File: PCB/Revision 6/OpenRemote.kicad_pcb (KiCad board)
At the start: 2 copper layers, 192.4 x 50 mm, 191 parts, among them J1 USB_C_Receptacle_USB2.0, J2 Conn_01x50, J3 JST_PH_B2B-PH, J4 2.54x2 Header, J5 Micro_SD_Card, Q1 DMG2301L, Q2 MBT3904DW1, Q3 DMG2301L, Q4 DMG2301L, Q5 DMG2301L, Q6 FS8205A, Q7 DMG2301L, U1 DW01A, U10 APX803S, U11 TP4056, U12 TCA8418, U2 XC6220B331, U3 CH340C, U4 USBLC6-2P6, U5 LIS3DHTR, U6 TSSP77038, U7 ESP32-S3-WROOM-1-N16R8, U8 AP2112K-3.3, U9 MAX17048G

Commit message: Add headerless microphone 3D model
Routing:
- net SW_D: track 78.1 -> 73.3 mm, vias 3 -> 1
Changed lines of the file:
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@@
 		)
 		(fp_text user "ACOUSTIC PORT"
-			(at 0 -3.9 90)
-			(layer "F.Fab")
+			(at 0 2.5 270)
+			(layer "B.SilkS")
 			(effects
 				(font
@@
 					(thickness 0.12)
 				)
+				(justify mirror)
 			)
 		)
@@
 		)
 		(embedded_fonts no)
+		(model "${KIPRJMOD}/project_libraries/3D-models/MS3625_Circular_Microphone_Module_No_Headers.step"
+			(offset
+				(xyz 0 0 0)
+			)
+			(scale
+				(xyz 1 1 1)
+			)
+			(rotate
+				(xyz -90 -0 -180)
+			)
+		)
 	)
 	(footprint "Resistor_SMD:R_0603_1608Metric"
@@
 	)
 	(segment
-		(start 140.5 117)
-		(end 138.5 115)
-		(width 0.3)
-		(layer "F.Cu")
-		(net "SW_D")
-	)
-	(segment
 		(start 131.25 118.6)
 		(end 131.8 118.6)
@@
 		(net "SW_D")
 	)
-	(segment
-		(start 140.5 117.5)
-		(end 140.5 117)
-		(width 0.3)
-		(layer "F.Cu")
-		(net "SW_D")
-	)
 	(via
 		(at 131.8 118.6)
@@
 		(net "SW_D")
 	)
-	(via
-		(at 140.5 117.5)
-		(size 0.8)
-		(drill 0.4)
-		(layers "F.Cu" "B.Cu")
-		(net "SW_D")
-	)
-	(via
-		(at 138.5 115)
-		(size 0.8)
-		(drill 0.4)
-		(layers "F.Cu" "B.Cu")
-		(net "SW_D")
-	)
-	(segment
-		(start 139.526677 118.6)
-		(end 140.5 117.626677)
-		(width 0.3)
-		(layer "B.Cu")
-		(net "SW_D")
-	)
 	(segment
 		(start 140.275 108.225)
@@
 		(width 0.3)
 		(layer "B.Cu")
-		(net "SW_D")
-	)
-	(segment
-		(start 140.5 117.626677)
-		(end 140.5 117.5)
-		(width 0.3)
-		(layer "B.Cu")

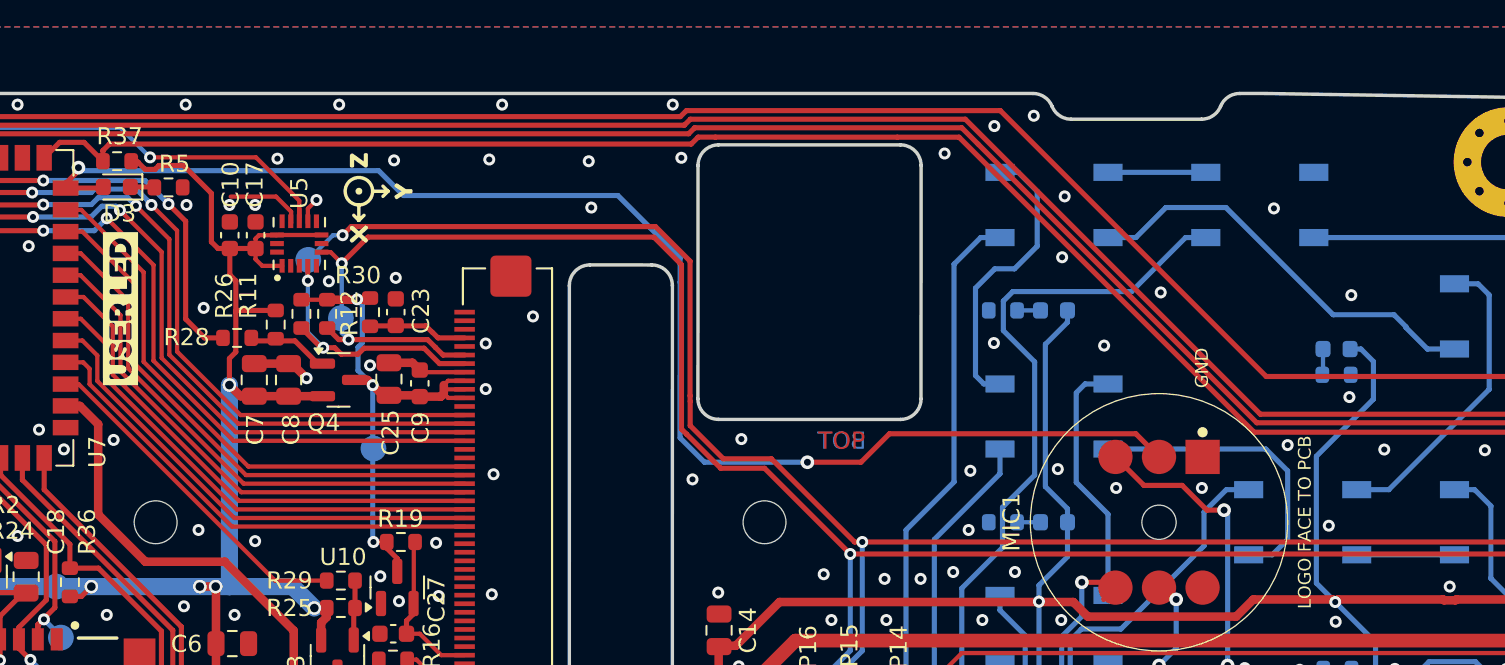
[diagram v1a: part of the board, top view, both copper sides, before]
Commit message: Add Rev 6 microphone and display updates
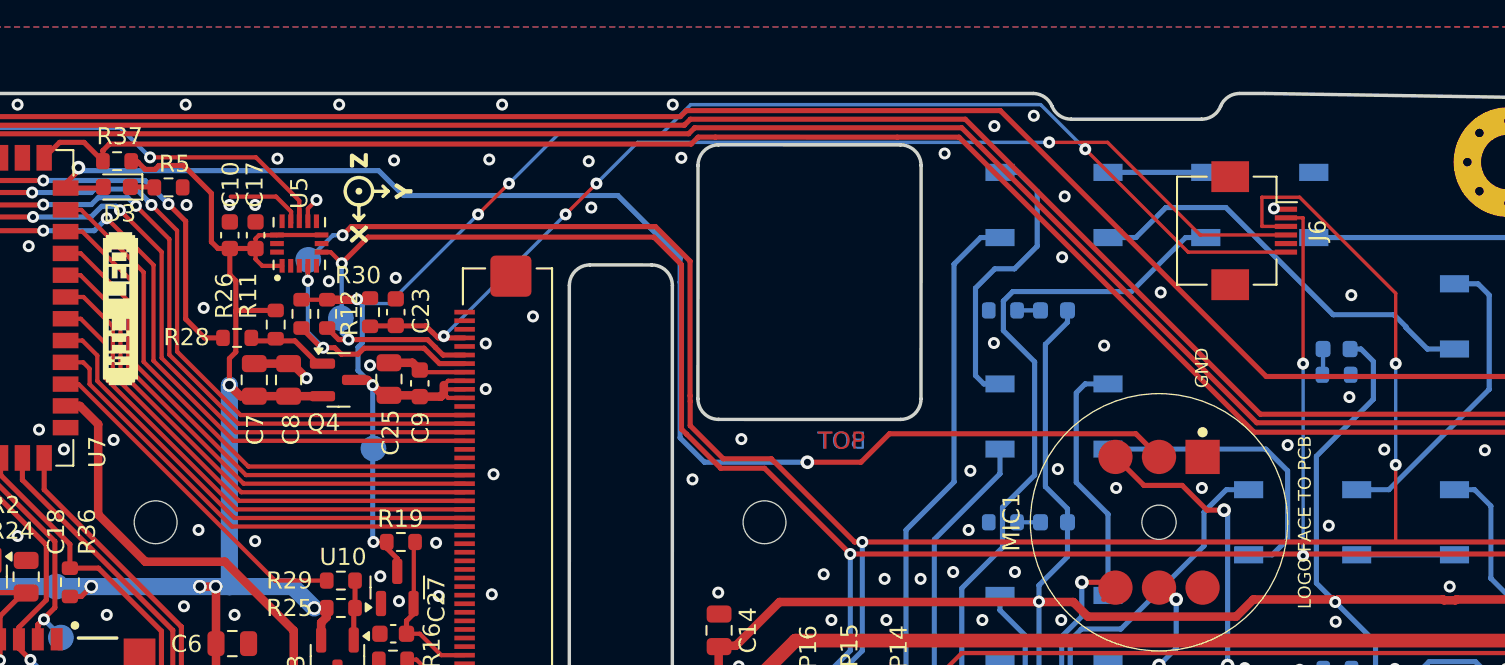
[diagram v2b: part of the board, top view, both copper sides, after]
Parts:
- added J6: ER-CON06HB-1_TOUCH, ER-CON06HB-1_Compatible_1x06_P0.50mm_BottomContact, F.Cu at (148.1, 85.0)
- added LCD1: Adafruit_280QV10_MECHANICAL, OpenRemoteLib:Adafruit_280QV10_MECHANICAL, F.Cu at (91.6, 102.0)
- added LCD2: ER-TFT028-4.2_MECHANICAL, ER-TFT028-4.2_MECHANICAL, B.Cu at (94.3, 102.0)
- MIC_LED_LABEL: renamed from kibuzzard-643EE46C; value G*** -> MIC LED; footprint kibuzzard-643EE46C -> OpenRemote:MIC_LED_LABEL
- OPENREMOTE_QR: renamed from G***; value LOGO -> https://github.com/LORDSn1per/OpenRemote-Hardware; footprint LOGO -> OpenRemote:OPENREMOTE_GITHUB_QR
- turned OPENREMOTE_QR to 90 degrees
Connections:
- net /TP_NRST renamed TP_NRST
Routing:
- net +VSW: track 31.5 -> 93.8 mm, vias 3 -> 6
- net TP_NRST: track 5.81 -> 62.0 mm, vias 0 -> 4
- net SCL: track 244.9 -> 272.7 mm, vias 5 -> 7
- net SDA: track 238.3 -> 259.1 mm, vias 4 -> 6
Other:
- board text added: "OpenRemote Rev. 6 Maximilian Kern & Phillip Carlson Aug 2026"
- board text removed: "OMOTE Rev. 5 Maximilian Kern 12/2024"
